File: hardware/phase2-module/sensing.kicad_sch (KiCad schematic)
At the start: 16 parts, among them U13 TMUX1101, U4 INA240A3, U5 INA228

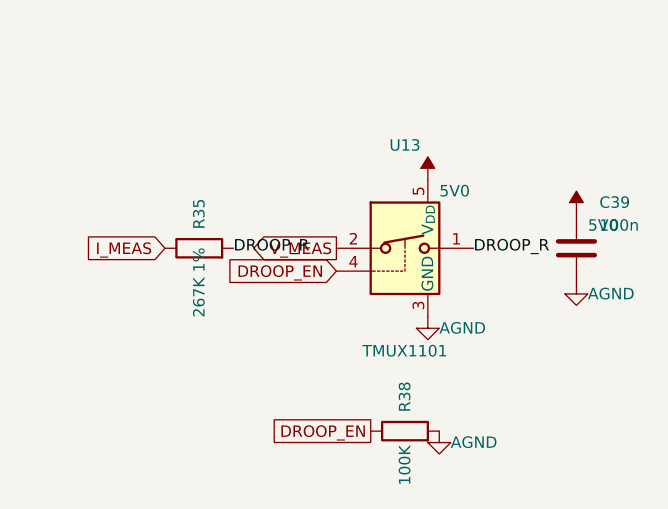
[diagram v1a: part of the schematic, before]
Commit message: Apply China-sourcing engineering changes across all boards + mechanical frame
All datasheet-verified before application (details hardware/SOURCING.md sF):
- TMUX1101 -> TS5A3166DBVR (LCSC availability; ts5a3166.pdf: pin POSITIONS
  identical - 1=NO 2=COM 3=GND 4=IN 5=V+; VIH 2.4V ok from 3.3V GPIO)
- TLV7011 DBVR -> DCKR: tlv7022.pdf shows DBV/DCK share one pinout, so
  footprint-only (SOT-353_SC-70-5); SOT-23-5 stock in China is nearly gone
- crystal load caps 10p -> 18p, both phases (CL=12pF China crystals; the
  HANDOVER-blessed alternative to hunting CL=8pF parts)
- Phase-1 inductor -> MWSA1707S-100MT (JLCPCB-verified 16.5A Isat/10.5A
  Irms vs 12A/8A required); value strings now dual-source Sunlord/Coilcraft
- module slot power + P2 output -> XT60PW-M (2-pin), backplane slots ->
  XT60PW-F; bus shunt -> 2x BVS-M-R0005 parallel (the exact-net checker
  caught RS1/RS2 placed one pin-span apart merging VBUS_IN into VBUS)
- 470u bulk -> THT radial D10; output MLCCs 22u -> 10u/50V X7S; buzzer ->
  MLT-8530 (fp placeholder)
All four checker chains green: 137/173/30/80 components.

hardware/MECHANICAL.md (frozen): 30mm slot pitch, P2 130x90 4-layer,
backplane ~330x100 2-layer 2oz, manager 100x80; cost-first stackup (1oz
outer + solder-reinforced bus, 2oz only if the thermal soak demands it);
inductor footprint = SUPERSET pattern accepting Sunlord 1707 AND Coilcraft
XAL1510 so the A/B pair is a pure part swap.

HANDOVER: sub-0.5V mV-accurate output DEFERRED to a future dedicated
linear post-regulator module (user decision 2026-07-18); buck floors
documented (P2 0.7V @30V bus, P1 0.5V).

Co-Authored-By: Claude Fable 5 <noreply@anthropic.com>
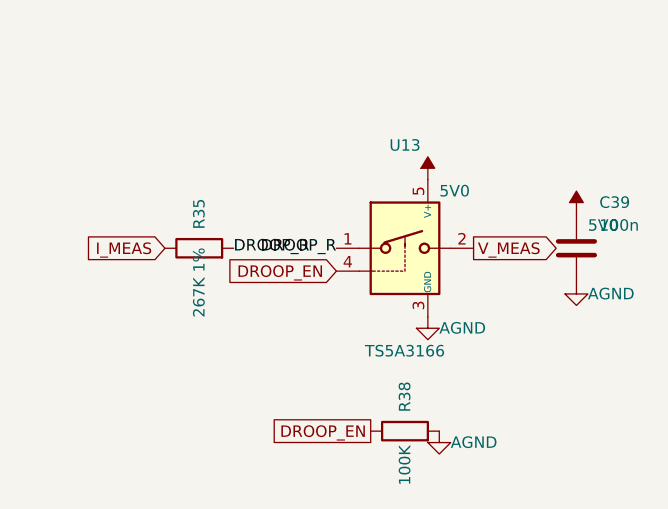
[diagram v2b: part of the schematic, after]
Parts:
- removed U13: TMUX1101, Package_TO_SOT_SMD:SOT-23-5, symbol Analog_Switch:TMUX1101DBV
- added U13: TS5A3166, Package_TO_SOT_SMD:SOT-23-5, symbol Analog_Switch:TS5A3166DBVR
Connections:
- net 5V0: now also U13.5 (V+)
- net AGND: now also U13.3 (GND)
- net DROOP_EN: now also U13.4
- net DROOP_R: now also U13.1
- net V_MEAS: now also U13.2
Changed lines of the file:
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@@
   (global_label "I_MEAS" (shape input) (at 199.39 152.4 180) (fields_autoplaced) (effects (font (size 1.27 1.27))))
   (label "DROOP_R" (at 207.01 152.4 0) (effects (font (size 1.27 1.27))))
-  (label "DROOP_R" (at 233.68 152.4 0) (effects (font (size 1.27 1.27))))
-  (global_label "V_MEAS" (shape output) (at 218.44 152.4 180) (fields_autoplaced) (effects (font (size 1.27 1.27))))
+  (label "DROOP_R" (at 218.44 152.4 180) (effects (font (size 1.27 1.27))))
+  (global_label "V_MEAS" (shape output) (at 233.68 152.4 0) (fields_autoplaced) (effects (font (size 1.27 1.27))))
   (global_label "DROOP_EN" (shape input) (at 218.44 154.94 180) (fields_autoplaced) (effects (font (size 1.27 1.27))))
   (global_label "DROOP_EN" (shape passive) (at 222.25 172.72 180) (fields_autoplaced) (effects (font (size 1.27 1.27))))
@@
     (instances (project "phase2-module" (path "/f47c11d2-88b1-4e02-9d3a-7f10a2c50001/f47c11d2-88b1-4e02-9d3a-7f10a2c50013" (reference "R35") (unit 1))))
   )
-  (symbol (lib_id "Analog_Switch:TMUX1101DBV") (at 226.06 152.4 0) (unit 1)
+  (symbol (lib_id "Analog_Switch:TS5A3166DBVR") (at 226.06 152.4 0) (unit 1)
     (in_bom yes) (on_board yes) (dnp no)
     (property "Reference" "U13" (at 226.06 140.97 0) (effects (font (size 1.27 1.27))))
-    (property "Value" "TMUX1101" (at 226.06 163.83 0) (effects (font (size 1.27 1.27))))
+    (property "Value" "TS5A3166" (at 226.06 163.83 0) (effects (font (size 1.27 1.27))))
     (property "Footprint" "Package_TO_SOT_SMD:SOT-23-5" (at 226.06 152.4 0) (effects (font (size 1.27 1.27)) hide))
     (property "Datasheet" "~" (at 226.06 152.4 0) (effects (font (size 1.27 1.27)) hide))
